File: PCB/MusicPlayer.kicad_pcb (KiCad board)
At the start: 4 copper layers, 0 parts

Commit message: fixed schematic errors
Accidentally set all SMD 0603 to SMD 0603 metric
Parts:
- added C1: 10u, Capacitor_SMD:C_0603_1608Metric, F.Cu at (82.5, 111.7)
- added C10: 100n, Capacitor_SMD:C_0603_1608Metric, F.Cu at (120.2, 116.3)
- added C11: 100n, Capacitor_SMD:C_0603_1608Metric, F.Cu at (120.2, 118.1)
- added C12: 100n, Capacitor_SMD:C_0603_1608Metric, F.Cu at (122.6, 114.6)
- added C13: 10n, Capacitor_SMD:C_0603_1608Metric, F.Cu at (120.9, 120.2)
- added C14: 10n, Capacitor_SMD:C_0603_1608Metric, F.Cu at (120.9, 122.7)
- added C15: 100n, Capacitor_SMD:C_0603_1608Metric, F.Cu at (72.6, 90.8)
- added C16: 100n, Capacitor_SMD:C_0603_1608Metric, F.Cu at (82.5, 120.4)
- added C17: 10u, Capacitor_SMD:C_0603_1608Metric, F.Cu at (126.5, 66.8)
- added C18: 100n, Capacitor_SMD:C_0603_1608Metric, F.Cu at (126.5, 68.6)
- added C19: 100n, Capacitor_SMD:C_0603_1608Metric, F.Cu at (126.5, 70.3)
- added C2: 2.2u, Capacitor_SMD:C_0603_1608Metric, F.Cu at (82.5, 113.4)
- added C20: 100n, Capacitor_SMD:C_0603_1608Metric, F.Cu at (126.5, 72.1)
- added C21: 100n, Capacitor_SMD:C_0603_1608Metric, F.Cu at (126.5, 73.8)
- added C22: 100n, Capacitor_SMD:C_0603_1608Metric, F.Cu at (126.5, 75.6)
- added C3: 100u, Capacitor_SMD:CP_Elec_10x10, F.Cu at (183.9, 52.3)
- added C4: 100n, Capacitor_SMD:C_0603_1608Metric, F.Cu at (82.5, 115.2)
- added C5: 10u, Capacitor_SMD:C_0603_1608Metric, F.Cu at (82.5, 116.9)
- added C6: 4.7u, Capacitor_SMD:C_0603_1608Metric, F.Cu at (82.5, 118.7)
- added C7: 4.7u, Capacitor_SMD:C_0603_1608Metric, F.Cu at (112.4, 135.7)
- added C8: 100n, Capacitor_SMD:C_0603_1608Metric, F.Cu at (112.4, 137.4)
- added C9: 100n, Capacitor_SMD:C_0603_1608Metric, F.Cu at (120.2, 114.6)
- added D1: LowBatt, LED_SMD:LED_0603_1608Metric, F.Cu at (82.7, 123.9)
- added D2: Charging, LED_SMD:LED_0603_1608Metric, F.Cu at (82.7, 125.7)
- added D3: MBR120VLSFT1G, CustomFootprints:D_SOD-123FL, F.Cu at (160.0, 62.7)
- added D4: MBR120VLSFT1G, CustomFootprints:D_SOD-123FL, F.Cu at (160.0, 69.1)
- added D5: ERROR, LED_SMD:LED_0603_1608Metric, F.Cu at (85.5, 93.3)
- added D6: PAUSE, LED_SMD:LED_0603_1608Metric, F.Cu at (78.9, 92.6)
- added D7: PLAY, LED_SMD:LED_0603_1608Metric, F.Cu at (78.9, 94.3)
- added H1: MountingHole, MountingHole:MountingHole_2.2mm_M2, F.Cu at (133.0, 101.9)
- added H2: MountingHole, MountingHole:MountingHole_2.2mm_M2, F.Cu at (133.0, 107.9)
- added H3: MountingHole, MountingHole:MountingHole_2.2mm_M2, F.Cu at (133.0, 113.8)
- added H4: MountingHole, MountingHole:MountingHole_2.2mm_M2, F.Cu at (133.0, 119.8)
- added J1: 3.7v LiPo, Connector_JST:JST_PH_S2B-PH-K_1x02_P2.00mm_Horizontal, F.Cu at (145.3, 53.1)
- added J2: USB_C_Receptacle_USB2.0_16P, Connector_USB:USB_C_Receptacle_G-Switch_GT-USB-7010ASV, F.Cu at (146.1, 87.1)
- added J3: SSD1306D, Connector_PinSocket_2.54mm:PinSocket_1x04_P2.54mm_Vertical, F.Cu at (176.1, 89.1)
- added J4: Conn_ST_STDC14, Connector_PinHeader_1.27mm:PinHeader_2x07_P1.27mm_Vertical_SMD, F.Cu at (115.8, 50.3)
- added L1: 6.8u, CustomFootprints:L_10.2x10, F.Cu at (158.0, 50.4)
- added Q1: MMBT2907ALT1HTSA1, Package_TO_SOT_SMD:SOT-23, F.Cu at (96.7, 119.3)
- added Q2: NMOS, Package_TO_SOT_SMD:SOT-23, F.Cu at (96.7, 123.8)
- added R1: 2.1M, Resistor_SMD:R_0603_1608Metric, F.Cu at (82.5, 122.2)
- added R11: 10k, Resistor_SMD:R_0603_1608Metric, F.Cu at (87.4, 113.4)
- added R12: 10k, Resistor_SMD:R_0603_1608Metric, F.Cu at (87.4, 115.2)
- added R13: 100k, Resistor_SMD:R_0603_1608Metric, F.Cu at (122.6, 116.3)
- added R14: 10k, Resistor_SMD:R_0603_1608Metric, F.Cu at (122.6, 118.1)
- added R15: 10k, Resistor_SMD:R_0603_1608Metric, F.Cu at (125.1, 114.6)
- added R16: 10k, Resistor_SMD:R_0603_1608Metric, F.Cu at (125.1, 116.3)
- added R17: 10k, Resistor_SMD:R_0603_1608Metric, F.Cu at (125.1, 118.1)
- added R18: 470, Resistor_SMD:R_0603_1608Metric, F.Cu at (72.6, 92.6)
- added R19: 470, Resistor_SMD:R_0603_1608Metric, F.Cu at (72.6, 94.3)
- added R2: 390k, Resistor_SMD:R_0603_1608Metric, F.Cu at (84.9, 111.7)
- added R20: 36.1, Resistor_SMD:R_0603_1608Metric, F.Cu at (72.6, 96.1)
- added R21: 2k, Resistor_SMD:R_0603_1608Metric, F.Cu at (112.4, 139.2)
- added R22: 2k, Resistor_SMD:R_0603_1608Metric, F.Cu at (112.4, 140.9)
- added R23: 10k, Resistor_SMD:R_0603_1608Metric, F.Cu at (87.4, 116.9)
- added R24: 5.1k, Resistor_SMD:R_0603_1608Metric, F.Cu at (126.5, 77.3)
- added R25: 5.1k, Resistor_SMD:R_0603_1608Metric, F.Cu at (126.5, 79.1)
- added R3: 1.8M, Resistor_SMD:R_0603_1608Metric, F.Cu at (84.9, 113.4)
- added R4: 200k, Resistor_SMD:R_0603_1608Metric, F.Cu at (84.9, 115.2)
- added R5: 100k, Resistor_SMD:R_0603_1608Metric, F.Cu at (84.9, 116.9)
- added R6: 620, Resistor_SMD:R_0603_1608Metric, F.Cu at (84.9, 118.7)
- added R7: 1.07k, Resistor_SMD:R_0603_1608Metric, F.Cu at (84.9, 120.4)
- added R8: 2k, Resistor_SMD:R_0603_1608Metric, F.Cu at (84.9, 122.2)
- added R9: 100k, Resistor_SMD:R_0603_1608Metric, F.Cu at (87.4, 111.7)
- added SW1: ON_OFF, CustomFootprints:MS-22D28-G, F.Cu at (145.8, 66.0)
- added SW2: RESET, CustomFootprints:GT-TZ084, F.Cu at (172.2, 70.6)
- added SW3: PLAY_PAUSE, CustomFootprints:GT-TZ084, F.Cu at (215.3, 87.9)
- added SW4: NEXT, CustomFootprints:GT-TZ084, F.Cu at (215.2, 78.8)
- added SW5: PREV, CustomFootprints:GT-TZ084, F.Cu at (215.3, 97.9)
- added SW6: RotaryEncoder, CustomFootprints:RotaryEncoder_Alps_EC11E_Vertical_H20mm, F.Cu at (202.9, 47.5)
- added U1: TPS61090, Package_DFN_QFN:Texas_RSA_VQFN-16-1EP_4x4mm_P0.65mm_EP2.7x2.7mm_ThermalVias, F.Cu at (169.9, 53.7)
- added U2: LD1117S33TR_SOT223, Package_TO_SOT_SMD:SOT-223-3_TabPin2, F.Cu at (185.7, 70.1)
- added U3: MCP73831T-2ACI/OT, Package_TO_SOT_SMD:SOT-23-5, F.Cu at (91.2, 125.6)
- added U4: STM32G031K8U6, Package_DFN_QFN:QFN-32-1EP_5x5mm_P0.5mm_EP3.45x3.45mm, F.Cu at (183.1, 87.6)
- added U5: Music Maker FeatherWing, CustomFootprints:Music_Maker_Feather_Wing, F.Cu at (166.4, 125.2)
- added U6: MAX17048G, Package_DFN_QFN:TDFN-8-1EP_2x2mm_P0.5mm_EP0.8x1.2mm, F.Cu at (150.1, 46.5)
- added U7: USBLC6-2P6, Package_TO_SOT_SMD:SOT-666, F.Cu at (154.0, 87.6)
- added U8: CH340C, Package_SO:SOIC-16_3.9x9.9mm_P1.27mm, F.Cu at (160.8, 86.5)
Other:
- rule pad_to_mask_clearance: 0.1 -> 0.05

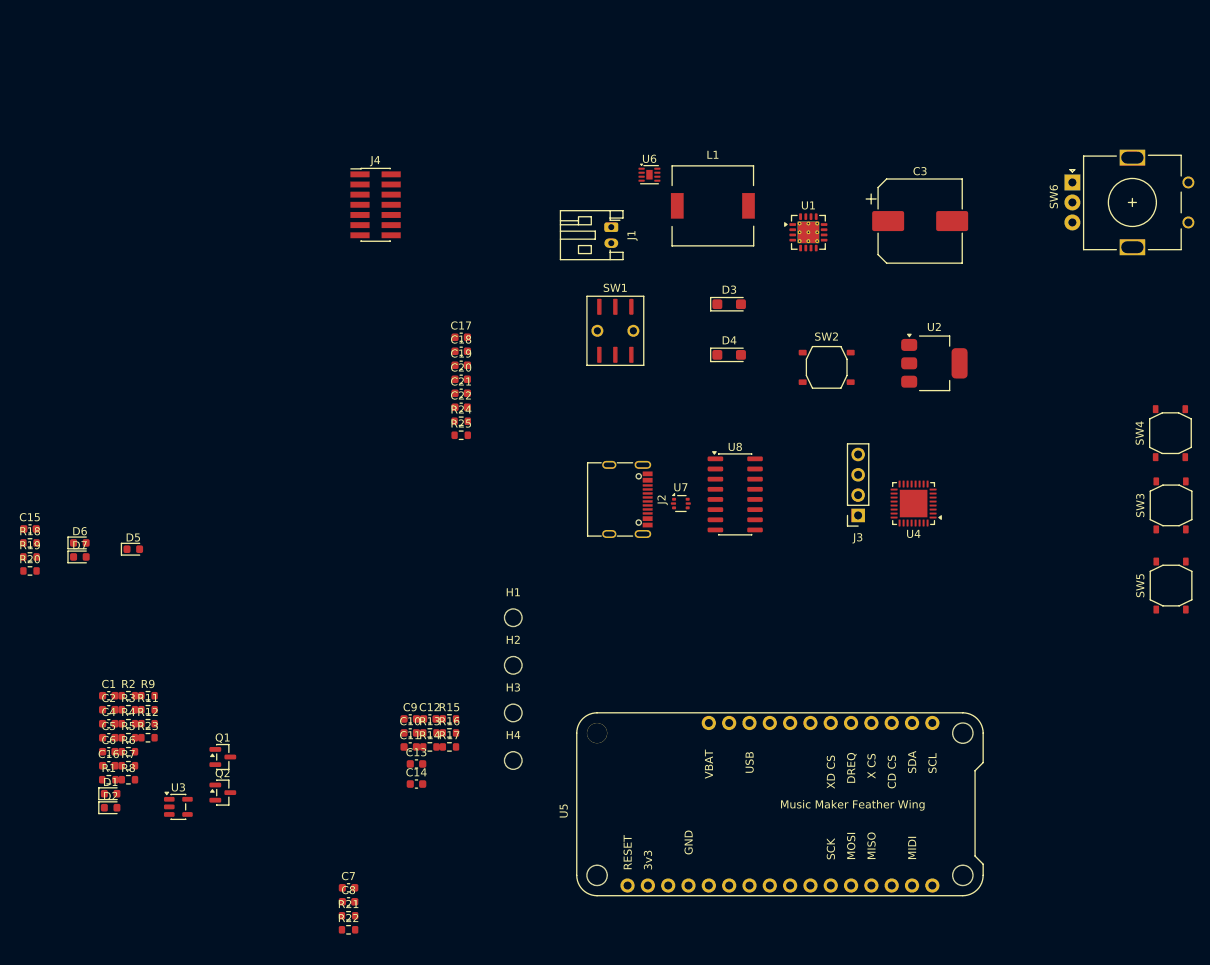
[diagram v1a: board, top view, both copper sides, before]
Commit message: Finished PCB parts layout
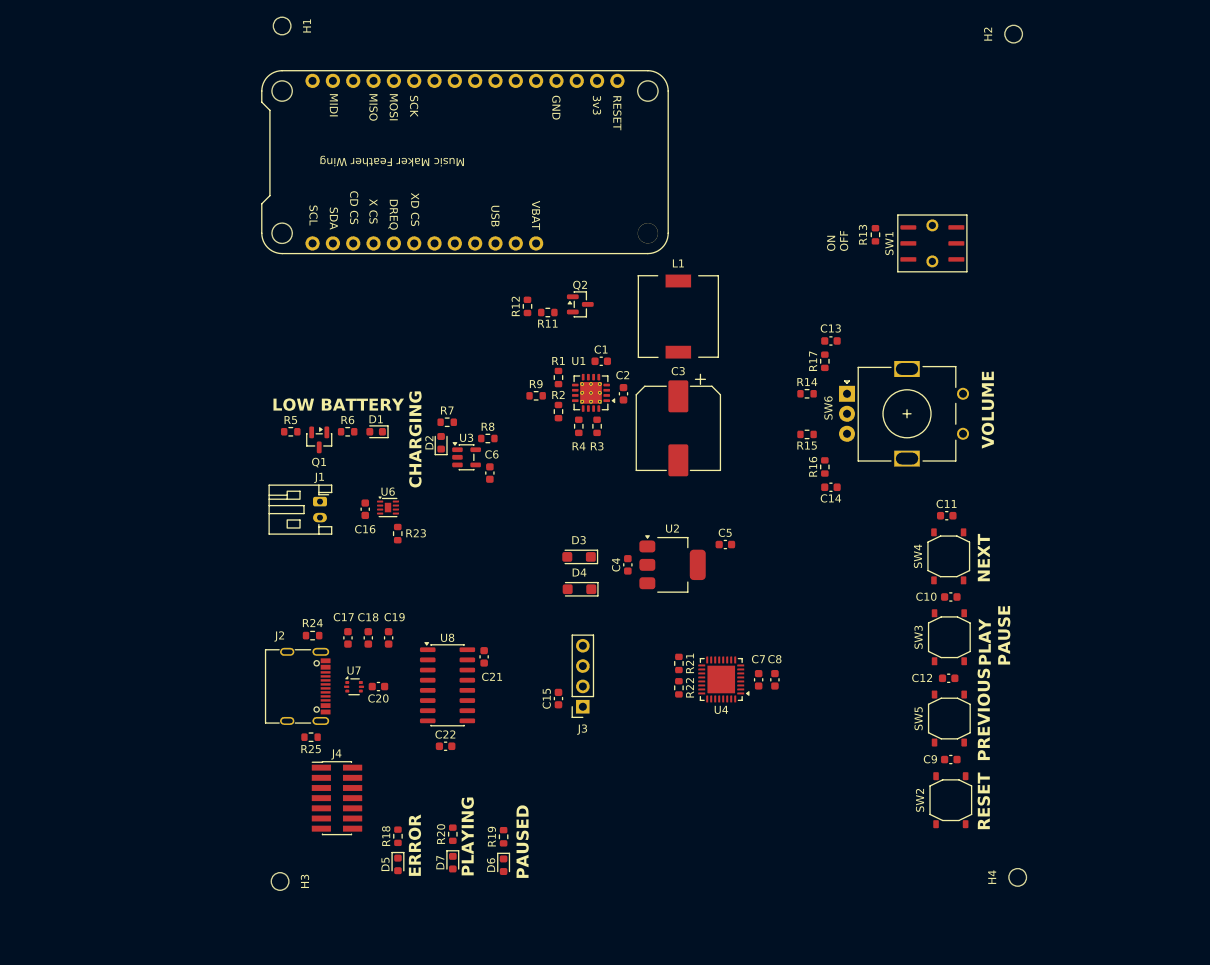
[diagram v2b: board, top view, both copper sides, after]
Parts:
- moved H2 100.7 mm to (195.6, 29.0), turned to 90 degrees
- moved U5 89.4 mm to (127.0, 45.0), turned to 180 degrees
- moved R13 83.5 mm to (178.3, 54.0), turned to 90 degrees
- moved C5 80.8 mm to (159.5, 92.8)
- moved H1 79.4 mm to (104.1, 27.9), turned to -90 degrees
- moved Q2 75.6 mm to (141.4, 62.7)
- moved C2 75.5 mm to (146.8, 73.9), turned to 90 degrees
- moved R1 75.4 mm to (138.7, 71.9), turned to -90 degrees
- moved C1 74.4 mm to (144.0, 69.8)
- moved J4 74.3 mm to (111.0, 124.5)
- moved C13 74.0 mm to (172.7, 67.3), turned to 180 degrees
- moved C11 73.0 mm to (187.2, 89.2)
- moved R12 70.5 mm to (134.8, 63.0), turned to 90 degrees
- moved R11 70.4 mm to (137.4, 63.8), turned to 180 degrees
- moved C10 69.7 mm to (187.7, 99.3)
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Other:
- board text added: "CHARGING"
- board text added: "ERROR"
- board text added: "LOW BATTERY"
- board text added: "NEXT"
- board text added: "ON OFF"
- board text added: "PAUSED"
- board text added: "PLAY PAUSE"
- board text added: "PLAYING"
- board text added: "PREVIOUS"
- board text added: "RESET"
- board text added: "VOLUME"

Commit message: Finished initial pcb routing
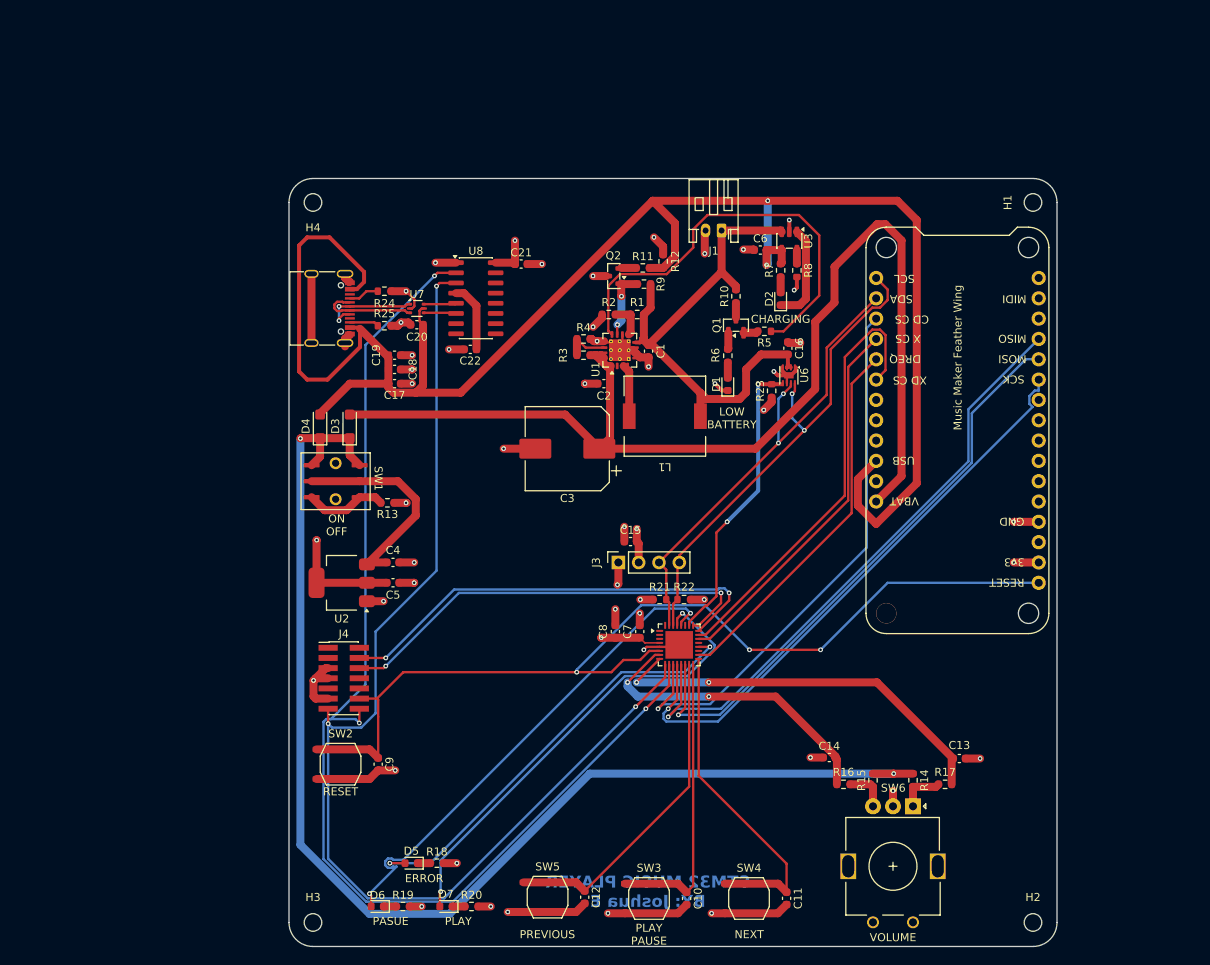
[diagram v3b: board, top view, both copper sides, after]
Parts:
- added R10: 0, Resistor_SMD:R_0603_1608Metric, F.Cu at (160.9, 61.7)
- U4: value STM32G031K8U6 -> STM32G031K8Ux
- moved H4 122.0 mm to (108.0, 50.0), turned to 180 degrees
- moved H2 111.1 mm to (198.0, 140.0), turned to 0 degrees
- moved H1 96.4 mm to (198.0, 50.0), turned to 90 degrees
- moved SW1 80.3 mm to (110.8, 84.8), turned to -90 degrees
- moved SW2 76.4 mm to (111.4, 120.2), turned to 0 degrees
- moved C9 71.6 mm to (116.1, 120.2), turned to -90 degrees
- moved U5 70.1 mm to (188.6, 78.5), turned to 90 degrees
- moved R13 69.6 mm to (117.3, 87.5), turned to 180 degrees
- moved J1 60.6 mm to (159.1, 53.5), turned to 180 degrees
- moved R5 60.5 mm to (164.4, 66.1), turned to 180 degrees
- moved C16 56.5 mm to (167.4, 68.2), turned to -90 degrees
- moved R17 55.0 mm to (187.0, 122.7), turned to 0 degrees
- moved SW5 55.0 mm to (137.3, 136.8), turned to 0 degrees
- moved C13 54.6 mm to (188.8, 119.5)
- moved Q1 54.0 mm to (160.9, 65.3), turned to 90 degrees
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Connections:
- J2 pad A6: /USB/USB_D+ -> /USB/D+
- J2 pad A7: /USB/USB_D- -> /USB/D-
- J2 pad B6: /USB/USB_D+ -> /USB/D+
- J2 pad B7: /USB/USB_D- -> /USB/D-
- U4 pad 1: BTN_PREV -> unconnected-(U4-PB9-Pad1)
- U4 pad 15: BTN_PLAY_PAUSE -> BTN_PREV
- U4 pad 16: ALRT -> BTN_PLAY_PAUSE
- U4 pad 17: unconnected-(U4-PB2-Pad17) -> BTN_NEXT
- U4 pad 18: unconnected-(U4-PA8-Pad18) -> DREQ
- U4 pad 19: SCL -> unconnected-(U4-NC/PA9-Pad19)
- U4 pad 21: SDA -> unconnected-(U4-NC/PA10-Pad21)
- U4 pad 26: unconnected-(U4-PA15-Pad26) -> ALRT
- U4 pad 27: DREQ -> unconnected-(U4-PB3-Pad27)
- U4 pad 30: unconnected-(U4-PB6-Pad30) -> SDA
- U4 pad 31: unconnected-(U4-PB7-Pad31) -> SCL
- U4 pad 32: BTN_NEXT -> unconnected-(U4-PB8-Pad32)
- U4 pad 4: GND -> +3V3
- U4 pad 5: +3V3 -> GND
- U4 pad 7: ENC_A -> ENC_B
- U4 pad 8: ENC_B -> ENC_A
- U7 pad 1: /USB/USB_D+ -> /USB/D+
- U7 pad 3: /USB/USB_D- -> /USB/D-
- U7 pad 4: /USB/USB_D- -> Net-(U8-UD-)
- U7 pad 6: /USB/USB_D+ -> Net-(U8-UD+)
- U8 pad 5: /USB/USB_D+ -> Net-(U8-UD+)
- U8 pad 6: /USB/USB_D- -> Net-(U8-UD-)
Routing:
- net VBUS: track 0.00 -> 226.0 mm, vias 0 -> 2
- net Diodes_5V: track 0.00 -> 154.7 mm, vias 0 -> 2
- net RX: track 0.00 -> 146.6 mm, vias 0 -> 3
- net TX: track 0.00 -> 142.0 mm, vias 0 -> 3
- net +5V: track 0.00 -> 139.9 mm
- net RESET: track 0.00 -> 122.8 mm, vias 0 -> 3
- net GND: track 0.00 -> 121.4 mm, vias 0 -> 40
- net MISO: track 0.00 -> 76.9 mm, vias 0 -> 1
- net SCK: track 0.00 -> 74.4 mm, vias 0 -> 1
- net MOSI: track 0.00 -> 73.7 mm, vias 0 -> 1
- net +3V3: track 0.00 -> 70.2 mm, vias 0 -> 11
- net SD_CS: track 0.00 -> 69.9 mm, vias 0 -> 1
- net +BATT: track 0.00 -> 67.3 mm
- net SDA: track 0.00 -> 62.4 mm, vias 0 -> 2
- net LED_PAUSED: track 0.00 -> 62.2 mm, vias 0 -> 2
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- added copper zone on In2.Cu, net +3V3
- added copper zone on In1.Cu, net GND
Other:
- board outline added: 96 x 96 mm
- board text added: "PASUE"
- board text added: "PLAY"
- board text added: "STM32 MUSIC PLAYER BY: Joshua E"
- board text removed: "PAUSED"
- board text removed: "PLAYING"
